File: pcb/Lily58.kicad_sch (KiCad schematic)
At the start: 118 parts, among them P3 ICSP, P4 OLED, SW1 SW_PUSH, SW10 SW_PUSH, SW11 SW_PUSH, SW12 SW_PUSH, SW13 SW_PUSH, SW14 SW_PUSH, SW15 SW_PUSH, SW16 SW_PUSH, SW17 SW_PUSH, SW18 SW_PUSH, SW19 SW_PUSH, SW2 SW_PUSH, SW20 SW_PUSH, SW21 SW_PUSH, SW22 SW_PUSH, SW23 SW_PUSH, SW24 SW_PUSH, SW25 Rotary_Encoder_Switch, SW26 SW_PUSH, SW27 SW_PUSH, SW28 SW_PUSH, SW29 SW_PUSH, SW3 SW_PUSH, SW4 SW_PUSH, SW5 SW_PUSH, SW6 SW_PUSH, SW7 SW_PUSH, SW8 SW_PUSH, SW9 SW_PUSH, U1 NiceNano

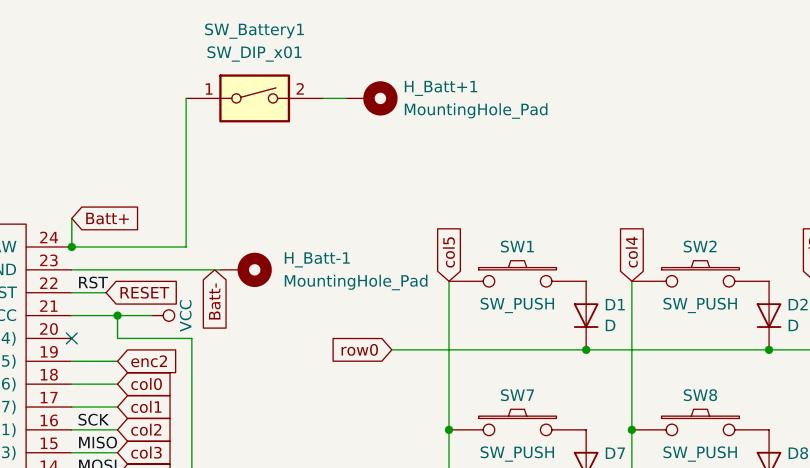
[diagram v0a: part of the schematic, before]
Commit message: Some file structure changes + lib files
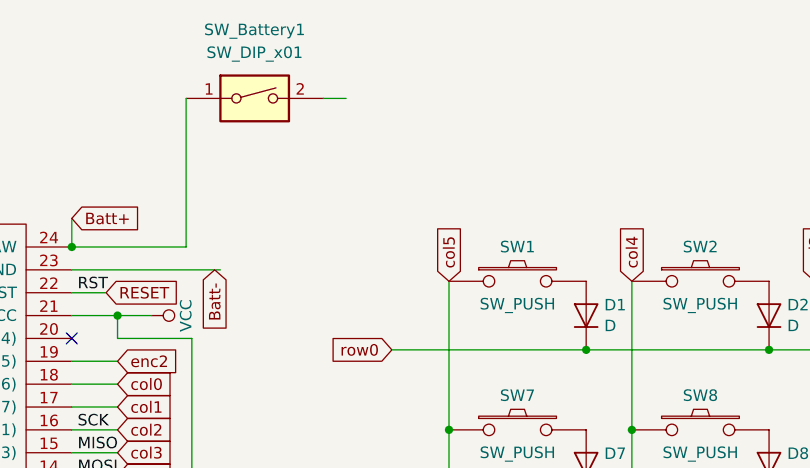
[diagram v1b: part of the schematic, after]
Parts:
- removed H_Batt+1, H_Batt-1: MountingHole_Pad, MountingHole:MountingHole_2.1mm, symbol Mechanical:MountingHole_Pad
- SW_LED1: footprint (none) -> AS13AH-KiCad:AS13AH
- U1: footprint Lily58-footprint:ProMicro_rev2 -> nice-nano-kicad:nice_nano
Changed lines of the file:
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@@
       (effects (font (size 1.524 1.524)))
     )
-    (property "Footprint" "Lily58-footprint:ProMicro_rev2" (id 2) (at 83.82 93.98 0)
+    (property "Footprint" "nice-nano-kicad:nice_nano" (id 2) (at 83.82 93.98 0)
       (effects (font (size 1.524 1.524)) hide)
     )
@@
     (pin "4")
   )
-  (symbol (lib_id "Mechanical:MountingHole_Pad") (at 116.84 55.88 270) (unit 1)
-    (in_bom yes) (on_board yes) (fields_autoplaced)
-    (property "Reference" "H_Batt-1" (id 0) (at 121.285 54.6099 90)
-      (effects (font (size 1.27 1.27)) (justify left))
-    )
-    (property "Value" "MountingHole_Pad" (id 1) (at 121.285 57.1499 90)
-      (effects (font (size 1.27 1.27)) (justify left))
-    )
-    (property "Footprint" "MountingHole:MountingHole_2.1mm" (id 2) (at 116.84 55.88 0)
-      (effects (font (size 1.27 1.27)) hide)
-    )
-    (property "Datasheet" "~" (id 3) (at 116.84 55.88 0)
-      (effects (font (size 1.27 1.27)) hide)
-    )
-    (pin "1")
-  )
   (symbol (lib_id "Switch:SW_DIP_x01") (at 118.11 36.83 0) (unit 1)
     (in_bom yes) (on_board yes) (fields_autoplaced)
@@
     (property "Reference" "SW_LED1" (id 0) (at 117.602 152.4 0))
     (property "Value" "SW_SPDT_MSM" (id 1) (at 117.602 154.94 0))
-    (property "Footprint" "" (id 2) (at 117.475 160.655 0)
+    (property "Footprint" "AS13AH-KiCad:AS13AH" (id 2) (at 117.475 160.655 0)
       (effects (font (size 1.27 1.27)) hide)
     )
@@
     (pin "1")
     (pin "2")
-  )
-  (symbol (lib_id "Mechanical:MountingHole_Pad") (at 130.81 36.83 270) (unit 1)
-    (in_bom yes) (on_board yes) (fields_autoplaced)
-    (property "Reference" "H_Batt+1" (id 0) (at 134.62 35.5599 90)
-      (effects (font (size 1.27 1.27)) (justify left))
-    )
-    (property "Value" "MountingHole_Pad" (id 1) (at 134.62 38.0999 90)
-      (effects (font (size 1.27 1.27)) (justify left))
-    )
-    (property "Footprint" "MountingHole:MountingHole_2.1mm" (id 2) (at 130.81 36.83 0)
-      (effects (font (size 1.27 1.27)) hide)
-    )
-    (property "Datasheet" "~" (id 3) (at 130.81 36.83 0)
-      (effects (font (size 1.27 1.27)) hide)
-    )
-    (pin "1")
   )
   (sheet_instances
@@
       (reference "D_LED1") (unit 1) (value "D") (footprint "Diode_THT:D_A-405_P7.62mm_Horizontal")
     )
-    (path "/d92b0bec-b24b-4172-8993-81116ed7c176"
-      (reference "H_Batt+1") (unit 1) (value "MountingHole_Pad") (footprint "MountingHole:MountingHole_2.1mm")
-    )
-    (path "/17c04d46-5545-49e7-a7ea-176e2d24b709"
-      (reference "H_Batt-1") (unit 1) (value "MountingHole_Pad") (footprint "MountingHole:MountingHole_2.1mm")
-    )
     (path "/00000000-0000-0000-0000-00005be6beda"
       (reference "JP1") (unit 1) (value "Jumper_NO_Small") (footprint "Lily58-footprint:Jumper")
@@
     )
     (path "/3c95667d-acb6-43db-817c-ce270389dbb5"
-      (reference "SW_LED1") (unit 1) (value "SW_SPDT_MSM") (footprint "")
+      (reference "SW_LED1") (unit 1) (value "SW_SPDT_MSM") (footprint "AS13AH-KiCad:AS13AH")
     )
     (path "/00000000-0000-0000-0000-00005b74ce27"
@@
     )
     (path "/00000000-0000-0000-0000-00005b722440"
-      (reference "U1") (unit 1) (value "NiceNano") (footprint "Lily58-footprint:ProMicro_rev2")
-    )
-  )
+      (reference "U1") (unit 1) (value "NiceNano") (footprint "nice-nano-kicad:nice_nano")
+    )
+  )

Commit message: Some more wiring updates
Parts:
- removed P3: ICSP, Lily58-footprint:ICSP, symbol Lily58-rescue:CONN_01X06-Lily58-cache
- added J+1, J-1: Conn_01x01_Male, TestPoint:TestPoint_Pad_2.0x2.0mm, symbol Connector:Conn_01x01_Male
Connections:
- net Batt-: now also J-1.1 (Pin_1)
- net at SW_Battery1.2: now also J+1.1 (Pin_1)
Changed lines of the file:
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@@
     (effects (font (size 1.27 1.27)) (justify left bottom))
   )
-  (label "MOSI" (at 66.04 134.62 0)
-    (effects (font (size 1.27 1.27)) (justify left bottom))
-  )
   (label "SCK" (at 98.425 73.66 0)
-    (effects (font (size 1.27 1.27)) (justify left bottom))
-  )
-  (label "MISO" (at 66.04 127 0)
-    (effects (font (size 1.27 1.27)) (justify left bottom))
-  )
-  (label "RST" (at 66.04 137.16 0)
-    (effects (font (size 1.27 1.27)) (justify left bottom))
-  )
-  (label "SCK" (at 66.04 132.08 0)
     (effects (font (size 1.27 1.27)) (justify left bottom))
   )
@@
     (pin "2")
   )
-  (symbol (lib_id "Lily58-rescue:CONN_01X06-Lily58-cache") (at 60.96 133.35 0) (mirror y) (unit 1)
-    (in_bom yes) (on_board yes)
-    (property "Reference" "P3" (id 0) (at 60.96 124.46 0))
-    (property "Value" "ICSP" (id 1) (at 60.96 142.24 0))
-    (property "Footprint" "Lily58-footprint:ICSP" (id 2) (at 60.96 133.35 0)
-      (effects (font (size 1.27 1.27)) hide)
-    )
-    (property "Datasheet" "" (id 3) (at 60.96 133.35 0))
-    (pin "1")
-    (pin "2")
-    (pin "3")
-    (pin "4")
-    (pin "5")
-    (pin "6")
-  )
-  (symbol (lib_id "power:VCC") (at 66.04 129.54 270) (unit 1)
-    (in_bom yes) (on_board yes)
-    (property "Reference" "#PWR0103" (id 0) (at 62.23 129.54 0)
-      (effects (font (size 1.27 1.27)) hide)
-    )
-    (property "Value" "VCC" (id 1) (at 69.2912 129.9718 90)
-      (effects (font (size 1.27 1.27)) (justify left))
-    )
-    (property "Footprint" "" (id 2) (at 66.04 129.54 0)
-      (effects (font (size 1.27 1.27)) hide)
-    )
-    (property "Datasheet" "" (id 3) (at 66.04 129.54 0)
-      (effects (font (size 1.27 1.27)) hide)
-    )
-    (pin "1")
-  )
-  (symbol (lib_id "power:GND") (at 66.04 139.7 0) (unit 1)
-    (in_bom yes) (on_board yes)
-    (property "Reference" "#PWR0104" (id 0) (at 66.04 146.05 0)
-      (effects (font (size 1.27 1.27)) hide)
-    )
-    (property "Value" "GND" (id 1) (at 66.167 144.0942 0))
-    (property "Footprint" "" (id 2) (at 66.04 139.7 0)
-      (effects (font (size 1.27 1.27)) hide)
-    )
-    (property "Datasheet" "" (id 3) (at 66.04 139.7 0)
-      (effects (font (size 1.27 1.27)) hide)
-    )
-    (pin "1")
-  )
   (symbol (lib_id "Lily58-rescue:CONN_01X04-Lily58-cache") (at 62.23 157.48 180) (unit 1)
     (in_bom yes) (on_board yes)
@@
     (pin "4")
   )
+  (symbol (lib_id "Connector:Conn_01x01_Male") (at 133.35 36.83 180) (unit 1)
+    (in_bom yes) (on_board yes) (fields_autoplaced)
+    (property "Reference" "J+1" (id 0) (at 132.715 31.75 0))
+    (property "Value" "Conn_01x01_Male" (id 1) (at 132.715 34.29 0))
+    (property "Footprint" "TestPoint:TestPoint_Pad_2.0x2.0mm" (id 2) (at 133.35 36.83 0)
+      (effects (font (size 1.27 1.27)) hide)
+    )
+    (property "Datasheet" "~" (id 3) (at 133.35 36.83 0)
+      (effects (font (size 1.27 1.27)) hide)
+    )
+    (pin "1")
+  )
   (symbol (lib_id "Switch:SW_DIP_x01") (at 118.11 36.83 0) (unit 1)
     (in_bom yes) (on_board yes) (fields_autoplaced)
@@
     (pin "2")
   )
+  (symbol (lib_id "Connector:Conn_01x01_Male") (at 119.38 55.88 180) (unit 1)
+    (in_bom yes) (on_board yes) (fields_autoplaced)
+    (property "Reference" "J-1" (id 0) (at 118.745 50.8 0))
+    (property "Value" "Conn_01x01_Male" (id 1) (at 118.745 53.34 0))
+    (property "Footprint" "TestPoint:TestPoint_Pad_2.0x2.0mm" (id 2) (at 119.38 55.88 0)
+      (effects (font (size 1.27 1.27)) hide)
+    )
+    (property "Datasheet" "~" (id 3) (at 119.38 55.88 0)
+      (effects (font (size 1.27 1.27)) hide)
+    )
+    (pin "1")
+  )
   (sheet_instances
     (path "/" (page "1"))
@@
       (reference "#PWR0102") (unit 1) (value "GND") (footprint "")
     )
-    (path "/00000000-0000-0000-0000-00005bb0f35d"
-      (reference "#PWR0103") (unit 1) (value "VCC") (footprint "")
-    )
-    (path "/00000000-0000-0000-0000-00005bb0f4c7"
-      (reference "#PWR0104") (unit 1) (value "GND") (footprint "")
-    )
     (path "/00000000-0000-0000-0000-00005d44c2b9"
       (reference "#PWR0105") (unit 1) (value "GND") (footprint "")
@@
       (reference "D_LED1") (unit 1) (value "D") (footprint "Diode_THT:D_A-405_P7.62mm_Horizontal")
     )
+    (path "/1c89b72b-aea2-4ed7-89d4-9ec742728b00"
+      (reference "J+1") (unit 1) (value "Conn_01x01_Male") (footprint "TestPoint:TestPoint_Pad_2.0x2.0mm")
+    )
+    (path "/9e37f993-417d-4daf-a341-38de2b4a2412"
+      (reference "J-1") (unit 1) (value "Conn_01x01_Male") (footprint "TestPoint:TestPoint_Pad_2.0x2.0mm")
+    )
     (path "/00000000-0000-0000-0000-00005be6beda"
       (reference "JP1") (unit 1) (value "Jumper_NO_Small") (footprint "Lily58-footprint:Jumper")
@@
       (reference "L36") (unit 1) (value "SK6812mini") (footprint "LED_SMD:LED_SK6812MINI_PLCC4_3.5x3.5mm_P1.75mm")
     )
-    (path "/00000000-0000-0000-0000-00005bb0ea73"
-      (reference "P3") (unit 1) (value "ICSP") (footprint "Lily58-footprint:ICSP")
-    )
     (path "/00000000-0000-0000-0000-00005be5032c"
